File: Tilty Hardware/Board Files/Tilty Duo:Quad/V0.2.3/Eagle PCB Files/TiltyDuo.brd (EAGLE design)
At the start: 38.1 x 50.8 mm, 44 parts, among them U1 TEENSY_3.0_OUTER-PINS28-DIP_S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, U2 HC-09_BREAKOUT, U3 MPL3115A2LGA8, U4 LM2931, U5 MPU-6050, U6 HMC5883LSMD, U7 SPI_FLASH-X25XXSMD

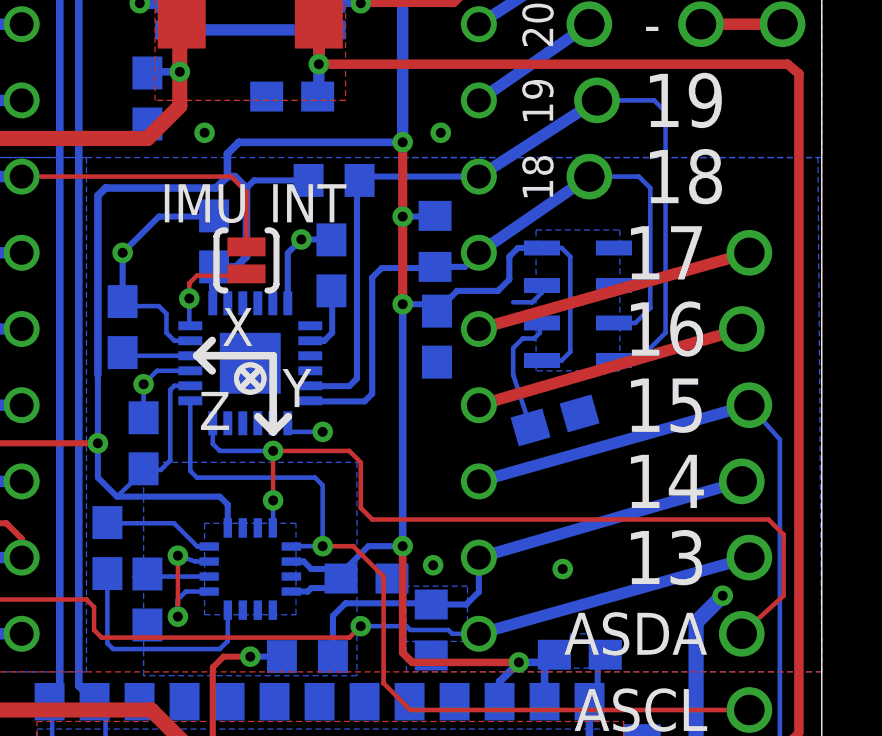
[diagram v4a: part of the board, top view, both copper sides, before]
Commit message: Updated Tilty Duo/Quad prototype so compass is no longer on Aux I2C bus
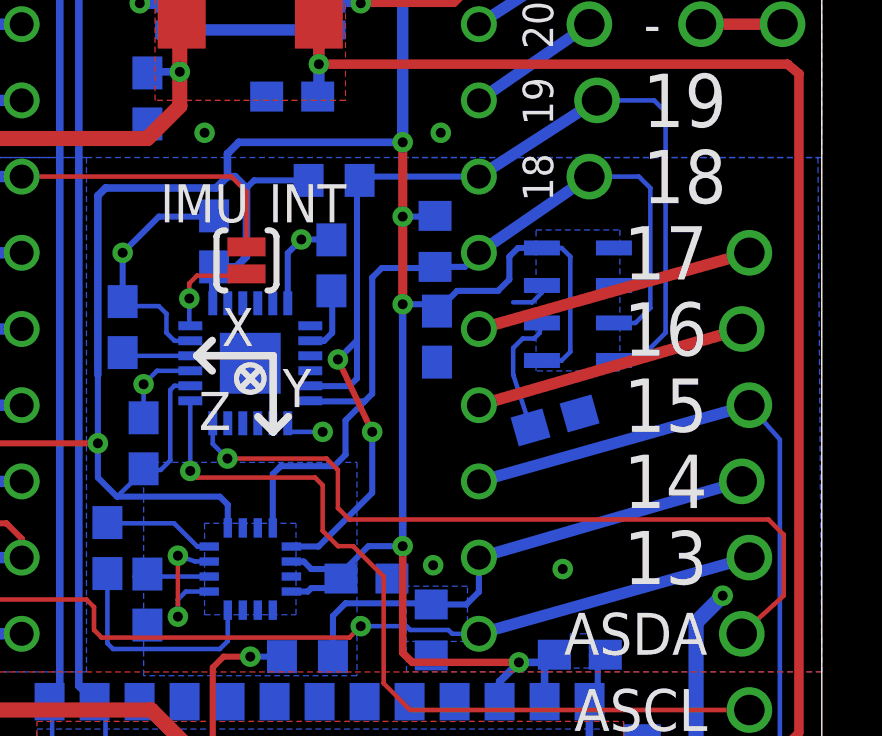
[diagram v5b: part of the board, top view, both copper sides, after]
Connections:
- net AUXCL: no longer U6.1
- net AUXDA: no longer U6.16
- net SCL: now also U6.1
- net SDA: now also U6.16
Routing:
- net SCL: track 29.1 -> 38.1 mm, vias 0 -> 2
- net SDA: track 22.0 -> 28.6 mm
- net AUXDA: track 28.4 -> 25.7 mm, vias 2 -> 1
- net AUXCL: track 28.6 -> 27.3 mm
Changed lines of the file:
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@@
 <wire x1="21.062" y1="24.638" x2="22.352" y2="24.638" width="0.2032" layer="16"/>
 <wire x1="22.352" y1="24.638" x2="22.606" y2="24.892" width="0.2032" layer="16"/>
-<wire x1="22.606" y1="24.892" x2="22.606" y2="31.408" width="0.2032" layer="16"/>
+<wire x1="22.606" y1="24.892" x2="22.606" y2="26.162" width="0.2032" layer="16"/>
+<wire x1="22.606" y1="26.162" x2="22.606" y2="31.408" width="0.2032" layer="16"/>
 <wire x1="26.67" y1="31.623" x2="22.821" y2="31.623" width="0.2032" layer="16"/>
 <wire x1="22.606" y1="31.408" x2="22.694" y2="31.496" width="0.2032" layer="16"/>
 <wire x1="22.821" y1="31.623" x2="22.694" y2="31.496" width="0.2032" layer="16"/>
+<contactref element="U6" pad="1"/>
+<via x="21.971" y="25.527" extent="1-16" drill="0.3302"/>
+<wire x1="21.971" y1="25.527" x2="22.606" y2="26.162" width="0.2032" layer="16"/>
+<via x="23.114" y="23.114" extent="1-16" drill="0.3302"/>
+<wire x1="23.114" y1="23.114" x2="21.971" y2="25.527" width="0.2032" layer="1"/>
+<wire x1="20.42" y1="19.292" x2="21.324" y2="19.292" width="0.2032" layer="16"/>
+<wire x1="21.324" y1="19.292" x2="23.114" y2="21.082" width="0.2032" layer="16"/>
+<wire x1="23.114" y1="21.082" x2="23.114" y2="23.114" width="0.2032" layer="16"/>
 </signal>
 <signal name="SDA" class="4">
@@
 <wire x1="25.2095" y1="28.614" x2="26.201" y2="28.614" width="0.2032" layer="16"/>
 <wire x1="26.201" y1="28.614" x2="26.67" y2="29.083" width="0.2032" layer="16"/>
+<contactref element="U6" pad="16"/>
+<wire x1="19.8" y1="19.912" x2="19.8" y2="21.705" width="0.2032" layer="16"/>
+<wire x1="19.8" y1="21.705" x2="20.066" y2="21.971" width="0.2032" layer="16"/>
+<wire x1="20.066" y1="21.971" x2="21.844" y2="21.971" width="0.2032" layer="16"/>
+<wire x1="21.844" y1="21.971" x2="22.225" y2="22.352" width="0.2032" layer="16"/>
+<wire x1="22.225" y1="22.352" x2="22.225" y2="23.495" width="0.2032" layer="16"/>
+<wire x1="22.225" y1="23.495" x2="22.86" y2="24.13" width="0.2032" layer="16"/>
 </signal>
 <signal name="N$1">
@@
 <signal name="AUXCL" class="4">
 <contactref element="U5" pad="7"/>
-<contactref element="U6" pad="1"/>
-<via x="21.463" y="19.304" extent="1-16" drill="0.3302"/>
 <wire x1="17.05" y1="24.15" x2="17.05" y2="21.812" width="0.1524" layer="16"/>
-<wire x1="17.05" y1="21.812" x2="17.272" y2="21.59" width="0.1524" layer="16"/>
-<wire x1="17.272" y1="21.59" x2="21.209" y2="21.59" width="0.1524" layer="16"/>
-<wire x1="21.209" y1="21.59" x2="21.463" y2="21.336" width="0.1524" layer="16"/>
-<wire x1="21.463" y1="21.336" x2="21.463" y2="19.304" width="0.1524" layer="16"/>
-<wire x1="21.463" y1="19.304" x2="20.432" y2="19.304" width="0.1524" layer="16"/>
-<wire x1="20.432" y1="19.304" x2="20.42" y2="19.292" width="0.1524" layer="16"/>
+<wire x1="17.05" y1="21.812" x2="17.272" y2="21.59" width="0.1524" layer="1"/>
+<wire x1="17.272" y1="21.59" x2="21.209" y2="21.59" width="0.1524" layer="1"/>
+<wire x1="21.209" y1="21.59" x2="21.463" y2="21.336" width="0.1524" layer="1"/>
 <contactref element="JP6" pad="2"/>
-<wire x1="21.463" y1="19.304" x2="22.479" y2="19.304" width="0.1524" layer="1"/>
 <wire x1="22.479" y1="19.304" x2="23.495" y2="18.288" width="0.1524" layer="1"/>
 <wire x1="23.495" y1="18.288" x2="23.495" y2="14.732" width="0.1524" layer="1"/>
 <wire x1="23.495" y1="14.732" x2="24.384" y2="13.843" width="0.1524" layer="1"/>
 <wire x1="24.384" y1="13.843" x2="35.687" y2="13.843" width="0.1524" layer="1"/>
+<via x="17.05" y="21.812" extent="1-16" drill="0.3302"/>
+<wire x1="22.479" y1="19.304" x2="21.971" y2="19.304" width="0.1524" layer="1"/>
+<wire x1="21.971" y1="19.304" x2="21.463" y2="19.812" width="0.1524" layer="1"/>
+<wire x1="21.463" y1="19.812" x2="21.463" y2="21.336" width="0.1524" layer="1"/>
 </signal>
 <signal name="AUXDA" class="4">
 <contactref element="U5" pad="6"/>
-<contactref element="U6" pad="16"/>
-<via x="19.812" y="22.479" extent="1-16" drill="0.3302"/>
-<via x="19.812" y="20.828" extent="1-16" drill="0.3302"/>
 <wire x1="17.78" y1="23.38" x2="17.8" y2="23.4" width="0.1524" layer="16"/>
 <contactref element="JP6" pad="3"/>
 <wire x1="17.8" y1="23.4" x2="17.8" y2="22.713" width="0.1524" layer="16"/>
-<wire x1="17.8" y1="22.713" x2="18.034" y2="22.479" width="0.1524" layer="16"/>
-<wire x1="18.034" y1="22.479" x2="19.812" y2="22.479" width="0.1524" layer="16"/>
-<wire x1="19.812" y1="20.828" x2="19.812" y2="19.924" width="0.1524" layer="16"/>
-<wire x1="19.812" y1="19.924" x2="19.8" y2="19.912" width="0.1524" layer="16"/>
-<wire x1="19.812" y1="20.828" x2="19.812" y2="22.479" width="0.1524" layer="1"/>
+<wire x1="17.8" y1="22.713" x2="18.288" y2="22.225" width="0.1524" layer="16"/>
 <wire x1="35.433" y1="16.383" x2="36.83" y2="17.653" width="0.1524" layer="1"/>
 <wire x1="36.83" y1="17.653" x2="36.83" y2="19.685" width="0.1524" layer="1"/>
 <wire x1="36.83" y1="19.685" x2="36.322" y2="20.193" width="0.1524" layer="1"/>
-<wire x1="36.322" y1="20.193" x2="23.114" y2="20.193" width="0.1524" layer="1"/>
-<wire x1="23.114" y1="20.193" x2="22.733" y2="20.574" width="0.1524" layer="1"/>
-<wire x1="22.733" y1="20.574" x2="22.733" y2="22.098" width="0.1524" layer="1"/>
-<wire x1="22.733" y1="22.098" x2="22.352" y2="22.479" width="0.1524" layer="1"/>
-<wire x1="22.352" y1="22.479" x2="19.812" y2="22.479" width="0.1524" layer="1"/>
+<wire x1="36.322" y1="20.193" x2="22.352" y2="20.193" width="0.1524" layer="1"/>
+<wire x1="22.352" y1="20.193" x2="21.971" y2="20.574" width="0.1524" layer="1"/>
+<wire x1="21.971" y1="20.574" x2="21.971" y2="21.844" width="0.1524" layer="1"/>
+<wire x1="21.971" y1="21.844" x2="21.59" y2="22.225" width="0.1524" layer="1"/>
+<wire x1="21.59" y1="22.225" x2="18.288" y2="22.225" width="0.1524" layer="1"/>
+<via x="18.288" y="22.225" extent="1-16" drill="0.3302"/>
 </signal>
 <signal name="RX3">

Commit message: Updated Tilty Duo/Quad PCB to have more parts on bottom of board
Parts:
- moved C4 10.1 mm to (23.1, 41.0), turned to 90 degrees
- moved C5 8.67 mm to (15.0, 41.0), turned to 90 degrees
- moved U4 2.73 mm to (19.1, 44.5), flipped to the bottom
- moved C13 1.27 mm to (7.62, 24.4), flipped to the bottom
- moved SJ2 0.51 mm to (16.5, 36.9)
- moved SJ3 0.51 mm to (21.6, 36.9)
- flipped U7 to the bottom, turned to 180 degrees
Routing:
- net 5V: track 83.4 -> 101.3 mm, vias 1 -> 2
- net VBATT: track 64.8 -> 72.6 mm
- net TEENSY_3V3: track 148.6 -> 143.4 mm, vias 6 -> 7
- net CS: track 15.8 -> 11.7 mm
- net GND: track 70.5 -> 68.7 mm, vias 22 -> 21
- net SCK: track 33.2 -> 31.6 mm, vias 1 -> 2
- net MISO: track 15.3 -> 15.8 mm
- removed copper zone on layer 1, net N$9

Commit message: Lots of little tweaks to perfect the Tilty Duo/Quad and updated ToDo list
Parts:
- added SJ4: SOLDERJUMPERTRACE, SparkFun-Passives:SJ_2S-TRACE
- JP8: device pinhead:1X02_NO_SS -> SparkFun-Passives:SJ_2S
- JP9: device pinhead:1X04 -> pinhead:1X04_NO_SS_LOCKING
- moved R4 6.31 mm to (36.4, 7.37), flipped to the bottom, turned to 90 degrees
- moved R3 4.72 mm to (33.7, 12.2), flipped to the bottom, turned to 270 degrees
- moved R8 2.47 mm to (33.7, 8.38), flipped to the bottom, turned to 270 degrees
- moved R7 1.69 mm to (35.1, 8.38)
- moved C13 1.14 mm to (7.11, 23.4), turned to 180 degrees
- moved JP8 0.90 mm to (36.6, 8.00), turned to 180 degrees
- moved C4 0.77 mm to (23.0, 40.3)
- moved C5 0.77 mm to (15.1, 40.3)
- moved R6 0.13 mm to (25.1, 16.4)
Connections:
- removed net AGND: U1.P$16
- new net N$9: R5.1, SJ4.2
- net GND: now also U1.P$16
- net VBATT: now also SJ4.1; no longer R5.1
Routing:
- net GND: track 68.7 -> 56.1 mm, vias 21 -> 28
- net N$13: track 1.80 -> 9.50 mm, vias 0 -> 1
- net N$9: track 0.00 -> 6.00 mm, vias 0 -> 1
- net CMD: track 29.1 -> 32.7 mm, vias 0 -> 1
- net N$24: track 1.93 -> 4.96 mm, vias 0 -> 1
- net N$3: track 2.03 -> 4.96 mm, vias 0 -> 1
- net SCL: track 38.1 -> 36.6 mm
- net SDA: track 28.6 -> 27.9 mm
- net BT_CMD: track 25.4 -> 26.0 mm, vias 0 -> 1
- net VBATT: track 72.6 -> 73.1 mm, vias 2 -> 1
- net 5V: track 101.3 -> 101.2 mm, vias 2 -> 1
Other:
- board text added: "July 2013"
- board text added: "Sense"
- board text added: "Voltage"
- board text added: "~"

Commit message: Slightly updated Tilty Duo/Quad PCB and added new prototype
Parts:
- renumbered JP8 to SJ5
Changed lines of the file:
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@@
 <element name="R5" library="resistor" package="R0603" value="10k" x="20.955" y="15.621" smashed="yes" rot="MR180"/>
 <element name="R6" library="resistor" package="R0603" value="680" x="25.0825" y="16.383" smashed="yes" rot="MR90"/>
-<element name="JP4" library="My Parts" package="2-POS_SMD_TERMINAL_BLOCK" value="2-POS_SMD_TERM_BLOCK" x="19.05" y="6.096"/>
+<element name="JP4" library="My Parts" package="2-POS_SMD_TERMINAL_BLOCK" value="2-POS_SMD_TERM_BLOCK" x="19.05" y="6.096">
+<attribute name="PART#" value="277-2337-1-ND" x="19.05" y="6.096" size="1.778" layer="27" display="off"/>
+<attribute name="POSSIBLE_ALT" value="009276002021106" x="19.05" y="6.096" size="1.778" layer="27" display="off"/>
+</element>
 <element name="U4" library="on-semiconductor" package="TO263" value="LM2931" x="19.05" y="44.5135" smashed="yes" rot="MR0">
 <attribute name="COST" value="0.53" x="19.05" y="44.5135" size="1.778" layer="28" rot="MR0" display="off"/>
@@
 <element name="U1" library="My Parts" package="28-DIP" value="TEENSY_3.0_OUTER-PINS28-DIP_SOCKET" x="19.05" y="32.893">
 <attribute name="COST" value="0.28" x="19.05" y="32.893" size="1.778" layer="27" display="off"/>
+<attribute name="PART#" value="AE10004-ND" x="19.05" y="32.893" size="1.778" layer="27" display="off"/>
+<attribute name="PART#2" value="A28-LC-TR-R" x="19.05" y="32.893" size="1.778" layer="27" display="off"/>
 </element>
 <element name="JP1" library="pinhead" package="1X08_NO_SS_LOCKING" value="" x="7.62" y="40.513" smashed="yes" rot="R90">
@@
 <element name="C12" library="resistor" package="C0603" value="0.1uF" x="25.273" y="26.289" smashed="yes" rot="MR90"/>
 <element name="U7" library="SparkFun-DigitalIC" package="SO08" value="SPI_FLASH-X25XXSMD" x="6.985" y="18.923" smashed="yes" rot="MR180">
-<attribute name="PART#" value="S25FL204K0TMFI011" x="6.985" y="18.923" size="1.778" layer="28" rot="MR180" display="off"/>
-<attribute name="PART#2" value="S25FL208K0RMFI011" x="6.985" y="18.923" size="1.778" layer="28" rot="MR180" display="off"/>
+<attribute name="PART#" value="S25FL204K0TMFI043" x="6.985" y="18.923" size="1.778" layer="28" rot="MR180" display="off"/>
 </element>
 <element name="C13" library="resistor" package="C0603" value="0.1uF" x="7.112" y="23.368" smashed="yes" rot="MR180">
@@
 <attribute name="VALUE" x="24.511" y="12.5095" size="0.4064" layer="27" rot="R90"/>
 </element>
-<element name="JP8" library="SparkFun-Passives" package="SJ_2S" value="" x="36.576" y="8.001" smashed="yes" rot="R180">
+<element name="SJ5" library="SparkFun-Passives" package="SJ_2S" value="" x="36.576" y="8.001" smashed="yes" rot="R180">
 <attribute name="VALUE" x="37.5258" y="9.652" size="0.4064" layer="27" rot="R180"/>
 </element>
@@
 <wire x1="12.3825" y1="1.8415" x2="13.589" y2="3.048" width="0.1524" layer="16"/>
 <wire x1="27.051" y1="3.048" x2="27.686" y2="3.683" width="0.1524" layer="16"/>
-<contactref element="JP8" pad="2"/>
+<contactref element="SJ5" pad="2"/>
 <via x="33.655" y="5.461" extent="1-16" drill="0.3302"/>
 <wire x1="33.3248" y1="4.6228" x2="27.94" y2="4.6228" width="0.1524" layer="16"/>
@@
 <contactref element="JP6" pad="6"/>
 <wire x1="26.67" y1="21.463" x2="35.687" y2="24.003" width="0.381" layer="16"/>
-<contactref element="JP8" pad="1"/>
+<contactref element="SJ5" pad="1"/>
 <wire x1="35.687" y1="24.003" x2="35.814" y2="24.003" width="0.1524" layer="16"/>
 <wire x1="35.814" y1="24.003" x2="36.957" y2="22.86" width="0.1524" layer="16"/>
@@
 </signal>
 </signals>
-<errors>
-</errors>
 </board>
 </drawing>
